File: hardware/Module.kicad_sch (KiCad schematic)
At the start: 47 parts, among them J1 CV_OUT, J10 POWER, J11 RIGHT, J2 CV2, J3 CV1, J4 CV3, J5 CV_TRIGGER, J6 CV_RSNX, J7 CV5, J8 CV4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

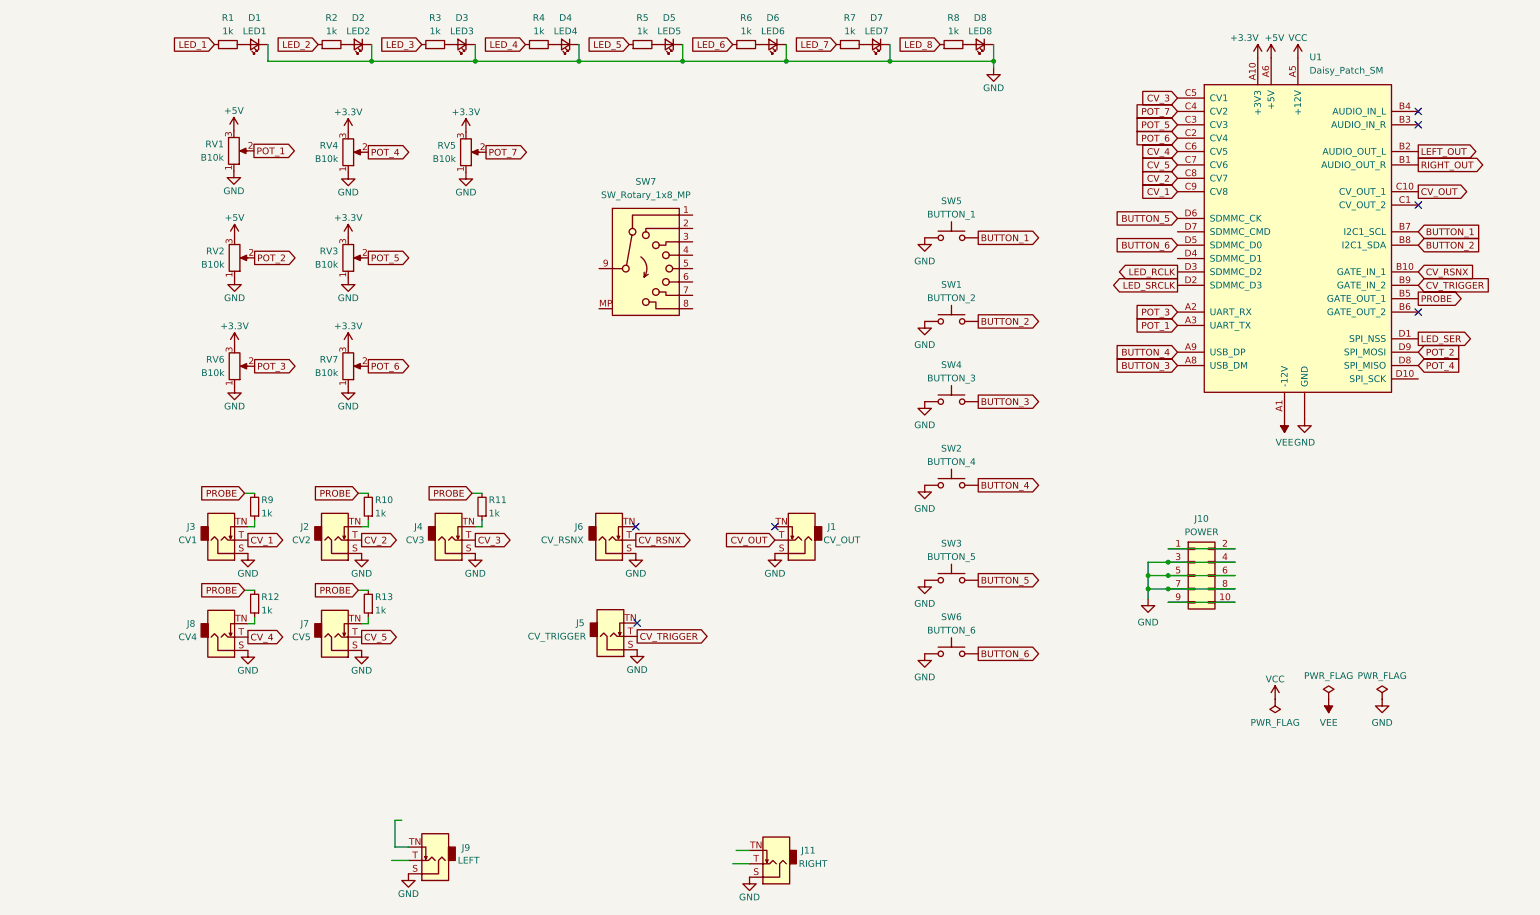
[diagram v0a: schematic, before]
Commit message: Patch a rough schematic
Signed-off-by: Petr Horacek <petr@zlosynth.com>
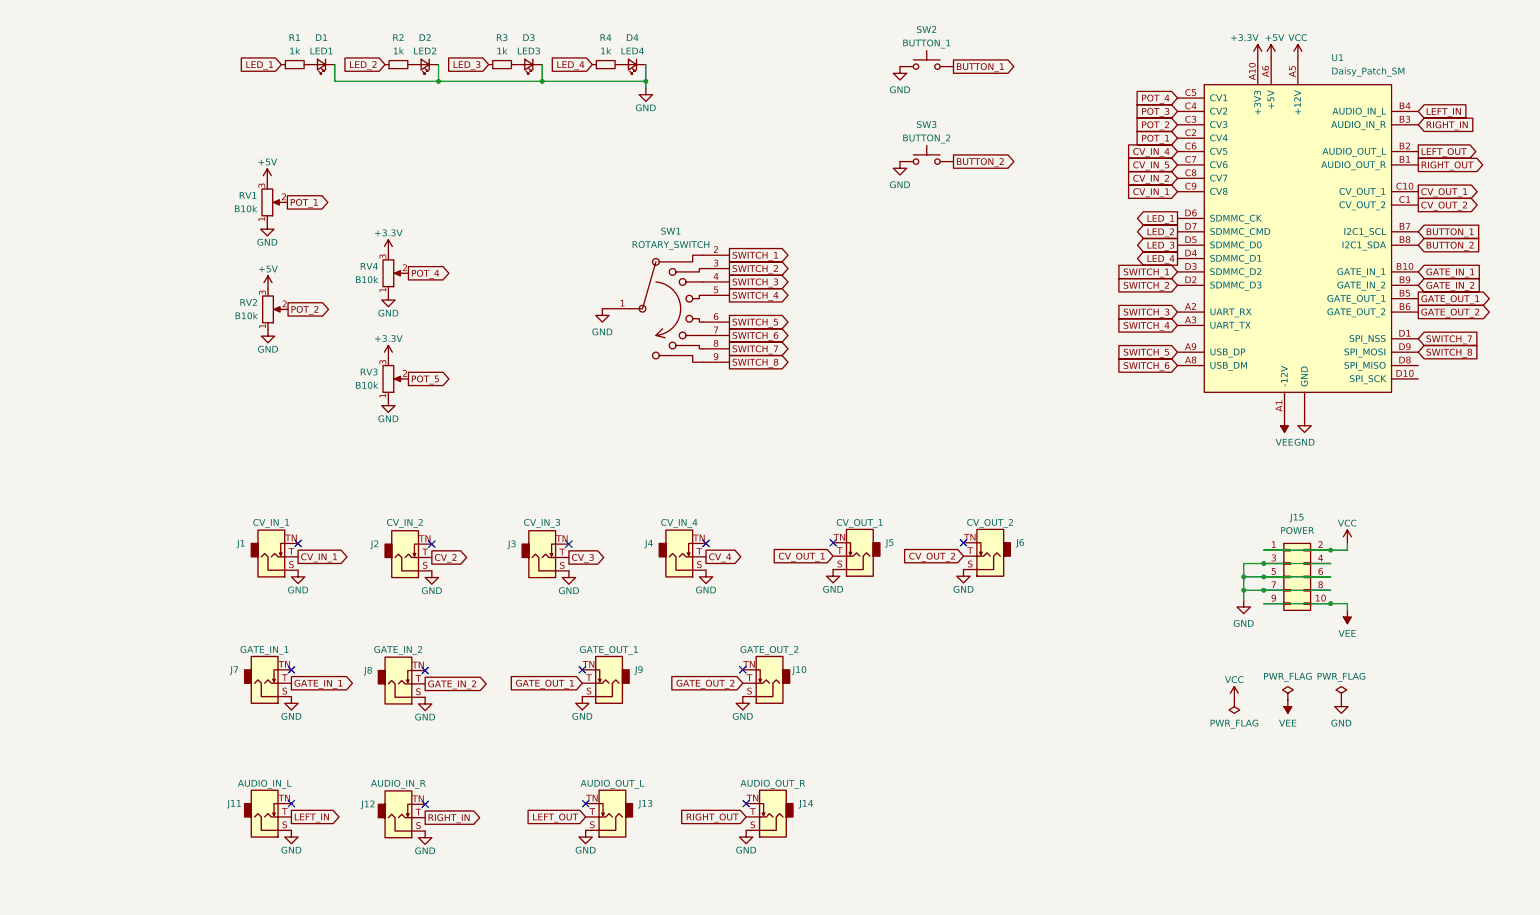
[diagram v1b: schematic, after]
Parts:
- removed D5: LED5, LED_THT:LED_D3.0mm, symbol Device:LED_Small
- removed D6: LED6, LED_THT:LED_D3.0mm, symbol Device:LED_Small
- removed D7: LED7, LED_THT:LED_D3.0mm, symbol Device:LED_Small
- removed D8: LED8, LED_THT:LED_D3.0mm, symbol Device:LED_Small
- removed J1: CV_OUT, Connector_Audio:Jack_3.5mm_QingPu_WQP-PJ398SM_Vertical_CircularHoles, symbol Connector_Audio:AudioJack2_SwitchT
- removed R10, R11, R12, R13, R5, R6, R7, R8, R9: 1k, Resistor_SMD:R_0805_2012Metric_Pad1.20x1.40mm_HandSolder, symbol Device:R_Small
- removed RV5, RV6, RV7: B10k, Custom:Potentiometer_Thonk_Trimmer, symbol Device:R_Potentiometer
- removed SW1: BUTTON_2, Button_Switch_THT:SW_PUSH_6mm, symbol Switch:SW_Push
- removed SW4: BUTTON_3, Button_Switch_THT:SW_PUSH_6mm, symbol Switch:SW_Push
- removed SW5: BUTTON_1, Button_Switch_THT:SW_PUSH_6mm, symbol Switch:SW_Push
- removed SW6: BUTTON_6, Button_Switch_THT:SW_PUSH_6mm, symbol Switch:SW_Push
- removed SW7: SW_Rotary_1x8_MP, Custom:Rotary_Switch_8_Alpha, symbol Switch:SW_Rotary_1x8_MP
- added J10: GATE_OUT_2, Connector_Audio:Jack_3.5mm_QingPu_WQP-PJ398SM_Vertical_CircularHoles, symbol Connector_Audio:AudioJack2_SwitchT
- added J12: AUDIO_IN_R, Connector_Audio:Jack_3.5mm_QingPu_WQP-PJ398SM_Vertical_CircularHoles, symbol Connector_Audio:AudioJack2_SwitchT
- added J13: AUDIO_OUT_L, Connector_Audio:Jack_3.5mm_QingPu_WQP-PJ398SM_Vertical_CircularHoles, symbol Connector_Audio:AudioJack2_SwitchT
- added J14: AUDIO_OUT_R, Connector_Audio:Jack_3.5mm_QingPu_WQP-PJ398SM_Vertical_CircularHoles, symbol Connector_Audio:AudioJack2_SwitchT
- added J8: GATE_IN_2, Connector_Audio:Jack_3.5mm_QingPu_WQP-PJ398SM_Vertical_CircularHoles, symbol Connector_Audio:AudioJack2_SwitchT
- added SW1: ROTARY_SWITCH, Custom:Rotary_Switch_8_Alpha, symbol Custom:SW_Rotary8
- J1: renamed from J3; value CV1 -> CV_IN_1
- J11: value RIGHT -> AUDIO_IN_L
- J2: value CV2 -> CV_IN_2
- J3: renamed from J4; value CV3 -> CV_IN_3
- J4: renamed from J8; value CV4 -> CV_IN_4
- J5: value CV_TRIGGER -> CV_OUT_1
- J6: value CV_RSNX -> CV_OUT_2
- J7: value CV5 -> GATE_IN_1
- J9: value LEFT -> GATE_OUT_1
- SW2: value BUTTON_4 -> BUTTON_1
- SW3: value BUTTON_5 -> BUTTON_2
- renumbered J10 to J15
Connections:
- net BUTTON_6 is gone; now on net LED_3: U1.D5 (SDMMC_D0)
- net POT_6 is gone; now on net POT_1: U1.C2 (CV4)
- net POT_7 is gone; now on net POT_3: U1.C4 (CV2)
- net PROBE is gone; now on net GATE_OUT_1: U1.B5 (GATE_OUT_1)
- net BUTTON_1: now also SW2.2
- net BUTTON_2: now also SW3.2
- net CV_2: no longer U1.C8 (CV7)
- net CV_3: no longer U1.C5 (CV1)
- net CV_4: no longer U1.C6 (CV5)
- net GND: now also J10.S, J12.S, J13.S, J14.S, J8.S, SW1.1
- net LED_1: now also U1.D6 (SDMMC_CK)
- net LED_2: now also U1.D7 (SDMMC_CMD)
- net LED_4: now also U1.D4 (SDMMC_D1)
- net LEFT_OUT: now also J13.T
- net POT_1: no longer U1.A3 (UART_TX)
- net POT_2: now also U1.C3 (CV3); no longer U1.D9 (SPI_MOSI)
- net POT_3: no longer U1.A2 (UART_RX)
- net POT_4: now also U1.C5 (CV1); no longer U1.D8 (SPI_MISO)
- net POT_5: no longer U1.C3 (CV3)
- net RIGHT_OUT: now also J14.T
- net VCC: now also J15.1 (Pin_1), J15.2 (Pin_2)
- net VEE: now also J15.10 (Pin_10), J15.9 (Pin_9)
- net LEFT_IN: now reaches J11.T
- net LEFT_IN: now also U1.B4 (AUDIO_IN_L)
- net RIGHT_IN: now reaches U1.B3 (AUDIO_IN_R)
- net RIGHT_IN: now also J12.T
- net GATE_OUT_2: now reaches U1.B6 (GATE_OUT_2)
- net GATE_OUT_2: now also J10.T
- net CV_OUT_2: now reaches U1.C1 (CV_OUT_2)
- net CV_OUT_2: now also J6.T
- net GATE_OUT_1: now reaches J9.T
- net BUTTON_3 renamed SWITCH_6
- net SWITCH_6: now also SW1.7
- net BUTTON_4 renamed SWITCH_5
- net SWITCH_5: now also SW1.6; no longer SW2.2
- removed net BUTTON_5: SW3.2, U1.D6 (SDMMC_CK)
- net CV_1 renamed CV_IN_1
- net CV_5 renamed CV_IN_5
- net CV_IN_5: no longer J7.T
- net CV_OUT renamed CV_OUT_1
- net CV_OUT_1: now also J5.T
- net CV_RSNX renamed GATE_IN_1
- net GATE_IN_1: now also J7.T; no longer J6.T
- net CV_TRIGGER renamed GATE_IN_2
- net GATE_IN_2: now also J8.T; no longer J5.T
- net LED_RCLK renamed SWITCH_1
- net SWITCH_1: now also SW1.2
- net LED_SER renamed SWITCH_7
- net SWITCH_7: now also SW1.8
- net LED_SRCLK renamed SWITCH_2
- net SWITCH_2: now also SW1.3
- new net CV_IN_2: U1.C8 (CV7)
- new net CV_IN_4: U1.C6 (CV5)
- new net SWITCH_3: SW1.4, U1.A2 (UART_RX)
- new net SWITCH_4: SW1.5, U1.A3 (UART_TX)
- new net SWITCH_8: SW1.9, U1.D9 (SPI_MOSI)
- no-connect marks 7 -> 14
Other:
- title: Arplus -> Handy
- moved on the sheet: D1, D2, D3, D4, J1, J15, J2, J3, J4, R1, R2, R3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

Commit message: First wire up of the PCB
Signed-off-by: Petr Horacek <petr@zlosynth.com>
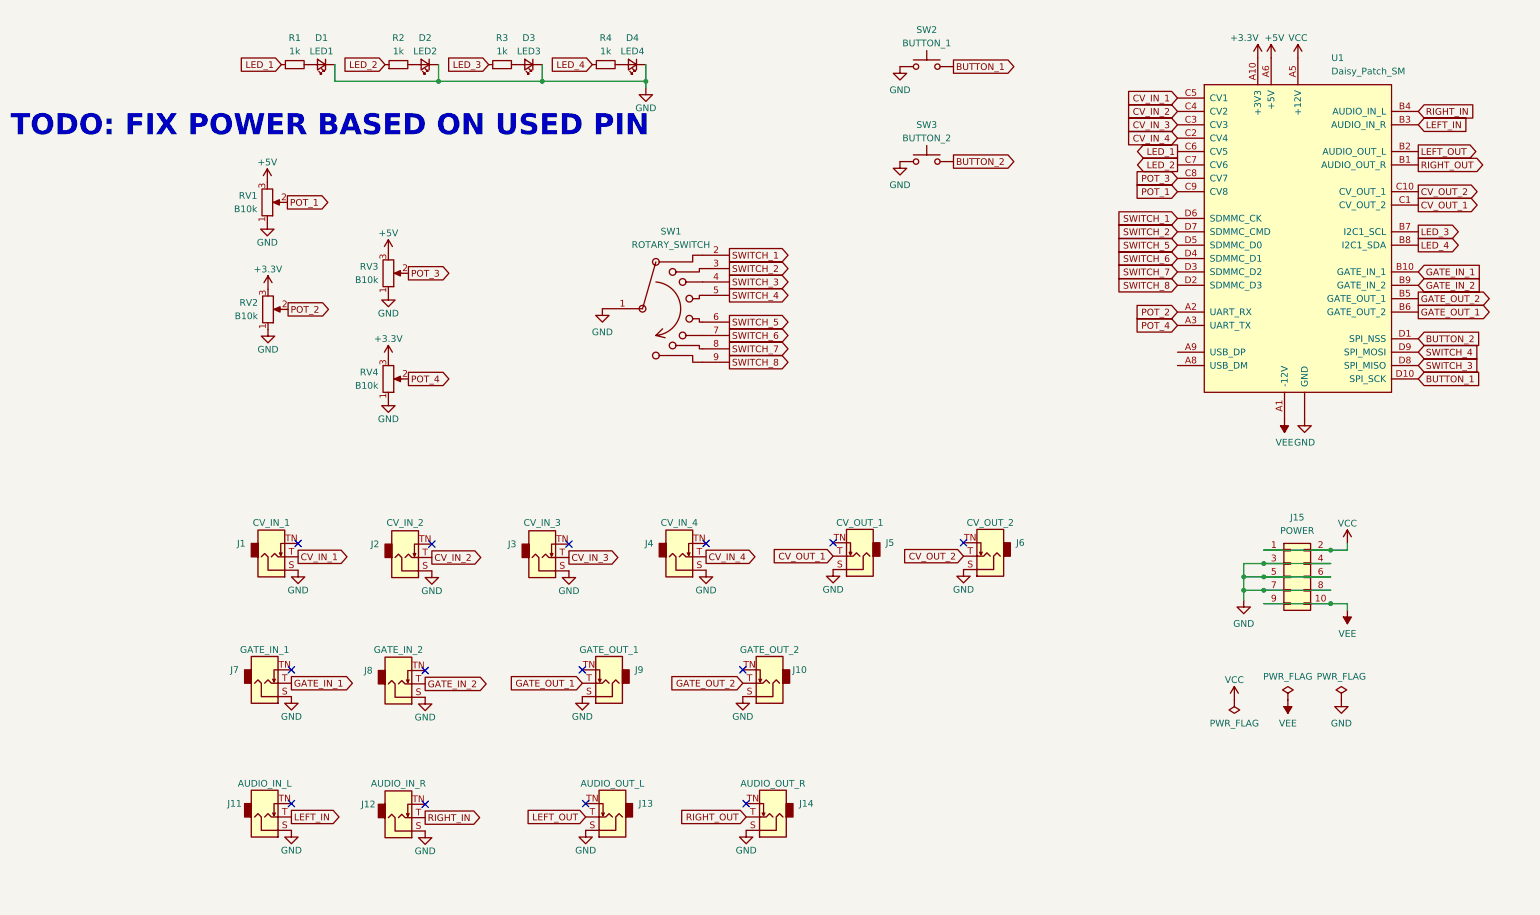
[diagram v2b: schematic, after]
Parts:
- renumbered RV4 to RV3, RV3 to RV4
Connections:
- net CV_2 is gone; now on net CV_IN_2: J2.T
- net CV_4 is gone; now on net CV_IN_4: J4.T
- net CV_IN_5 is gone; now on net LED_2: U1.C7 (CV6)
- net POT_5 is gone; now on net POT_4: RV4.2
- net +3.3V: now also RV2.3; no longer RV3.3
- net +5V: now also RV3.3; no longer RV2.3
- net BUTTON_1: now also U1.D10 (SPI_SCK); no longer U1.B7 (I2C1_SCL)
- net BUTTON_2: now also U1.D1 (SPI_NSS); no longer U1.B8 (I2C1_SDA)
- net CV_IN_1: now also U1.C5 (CV1); no longer U1.C9 (CV8)
- net CV_IN_2: now also U1.C4 (CV2); no longer U1.C8 (CV7)
- net CV_IN_4: now also U1.C2 (CV4); no longer U1.C6 (CV5)
- net CV_OUT_1: now also U1.C1 (CV_OUT_2); no longer U1.C10 (CV_OUT_1)
- net CV_OUT_2: now also U1.C10 (CV_OUT_1); no longer U1.C1 (CV_OUT_2)
- net GATE_OUT_1: now also U1.B6 (GATE_OUT_2); no longer U1.B5 (GATE_OUT_1)
- net GATE_OUT_2: now also U1.B5 (GATE_OUT_1); no longer U1.B6 (GATE_OUT_2)
- net LED_1: now also U1.C6 (CV5); no longer U1.D6 (SDMMC_CK)
- net LED_2: no longer U1.D7 (SDMMC_CMD)
- net LED_3: now also U1.B7 (I2C1_SCL); no longer U1.D5 (SDMMC_D0)
- net LED_4: now also U1.B8 (I2C1_SDA); no longer U1.D4 (SDMMC_D1)
- net LEFT_IN: now also U1.B3 (AUDIO_IN_R); no longer U1.B4 (AUDIO_IN_L)
- net POT_1: now also U1.C9 (CV8); no longer U1.C2 (CV4)
- net POT_2: now also U1.A2 (UART_RX); no longer U1.C3 (CV3)
- net POT_3: now also RV3.2, U1.C8 (CV7); no longer U1.C4 (CV2)
- net POT_4: now also U1.A3 (UART_TX); no longer RV3.2, U1.C5 (CV1)
- net RIGHT_IN: now also U1.B4 (AUDIO_IN_L); no longer U1.B3 (AUDIO_IN_R)
- net SWITCH_1: now also U1.D6 (SDMMC_CK); no longer U1.D3 (SDMMC_D2)
- net SWITCH_2: now also U1.D7 (SDMMC_CMD); no longer U1.D2 (SDMMC_D3)
- net SWITCH_3: now also U1.D8 (SPI_MISO); no longer U1.A2 (UART_RX)
- net SWITCH_4: now also U1.D9 (SPI_MOSI); no longer U1.A3 (UART_TX)
- net SWITCH_5: now also U1.D5 (SDMMC_D0); no longer U1.A9 (USB_DP)
- net SWITCH_6: now also U1.D4 (SDMMC_D1); no longer U1.A8 (USB_DM)
- net SWITCH_7: now also U1.D3 (SDMMC_D2); no longer U1.D1 (SPI_NSS)
- net SWITCH_8: now also U1.D2 (SDMMC_D3); no longer U1.D9 (SPI_MOSI)
- net CV_3 renamed CV_IN_3
- net CV_IN_3: now also U1.C3 (CV3)
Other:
- note added: "TODO: FIX POWER BASED ON USED PIN"

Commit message: Complete the ground plane and fix ERC
Signed-off-by: Petr Horacek <petr@zlosynth.com>
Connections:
- no-connect marks 14 -> 16
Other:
- note removed: "TODO: FIX POWER BASED ON USED PIN"

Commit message: Fix trimmer footprint
Signed-off-by: Petr Horacek <petr@zlosynth.com>
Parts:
- RV1, RV3: footprint Potentiometer_THT:Potentiometer_Alpha_RD901F-40-00D_Single_Vertical -> Custom:Potentiometer_Thonk_Trimmer
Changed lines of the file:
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@@
       (effects (font (size 1.27 1.27)) (justify right))
     )
-    (property "Footprint" "Potentiometer_THT:Potentiometer_Alpha_RD901F-40-00D_Single_Vertical" (at 34.163 56.007 0)
+    (property "Footprint" "Custom:Potentiometer_Thonk_Trimmer" (at 34.163 56.007 0)
       (effects (font (size 1.27 1.27)) hide)
     )
@@
       (effects (font (size 1.27 1.27)) (justify right))
     )
-    (property "Footprint" "Potentiometer_THT:Potentiometer_Alpha_RD901F-40-00D_Single_Vertical" (at 57.15 69.469 0)
-      (effects (font (size 1.27 1.27)) hide)
-    )
+    (property "Footprint" "Custom:Potentiometer_Thonk_Trimmer" (at 57.15 69.469 0)
+      (effects (font (size 1.27 1.27)) hide)
+    )

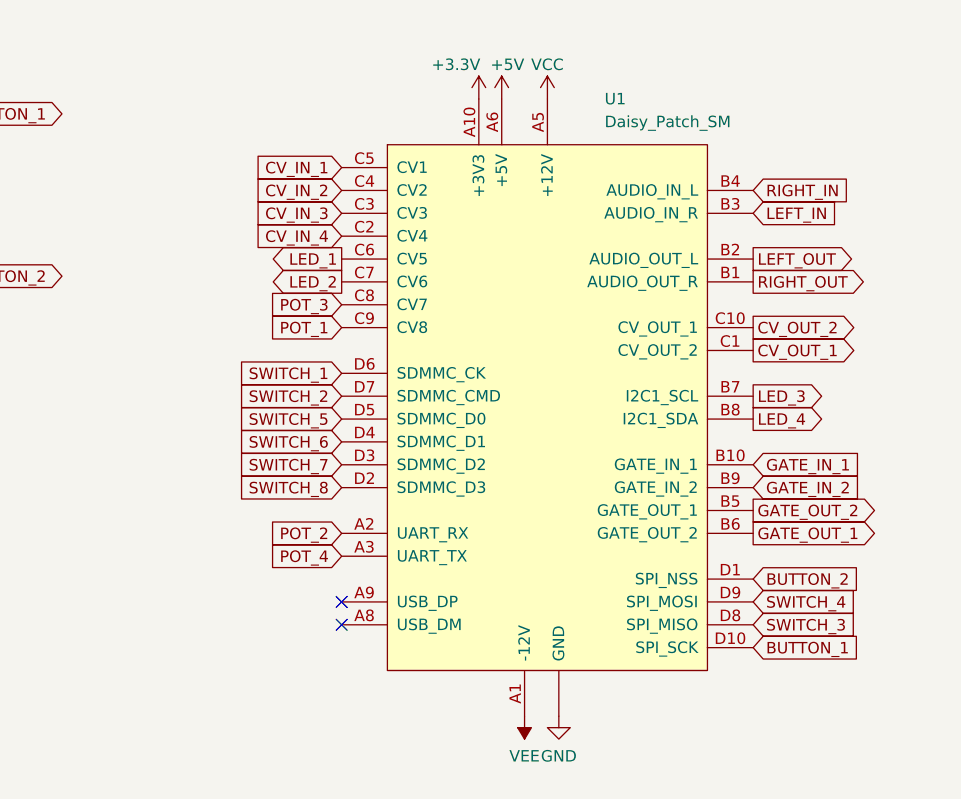
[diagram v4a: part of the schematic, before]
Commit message: Fix LED daisy connection
Signed-off-by: Petr Horacek <petr@zlosynth.com>
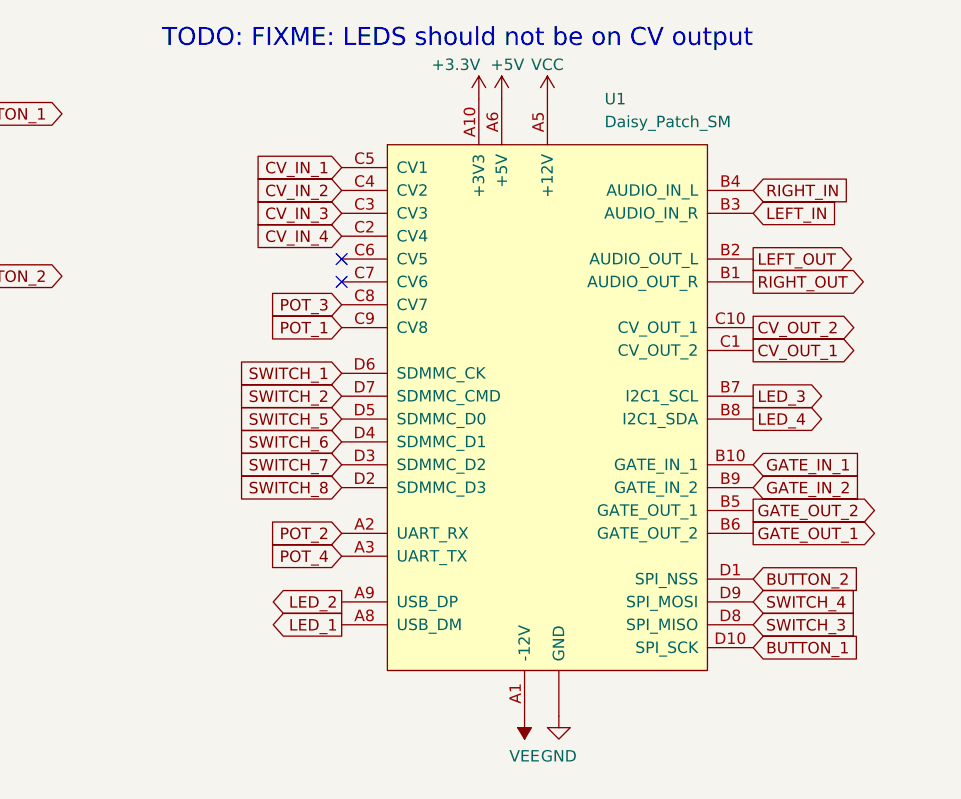
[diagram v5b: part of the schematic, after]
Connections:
- net LED_1: now also U1.A8 (USB_DM); no longer U1.C6 (CV5)
- net LED_2: now also U1.A9 (USB_DP); no longer U1.C7 (CV6)
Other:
- note added: "TODO: FIXME: LEDS should not be on CV output"
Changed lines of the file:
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@@
   (no_connect (at 141.732 120.65))
   (no_connect (at 64.262 170.434))
+  (no_connect (at 207.01 48.895))
   (no_connect (at 117.602 120.904))
   (no_connect (at 40.132 120.904))
+  (no_connect (at 207.01 46.355))
   (no_connect (at 65.532 120.904))
-  (no_connect (at 207.01 84.455))
   (no_connect (at 91.44 120.904))
   (no_connect (at 166.37 120.65))
   (no_connect (at 64.262 145.034))
   (no_connect (at 38.862 144.78))
-  (no_connect (at 207.01 86.995))
   (no_connect (at 124.46 144.78))
   (no_connect (at 125.222 170.18))
@@
     (stroke (width 0) (type default))
   )
+  (text "TODO: FIXME: LEDS should not be on CV output" (at 187.0456 23.0632 0)
+    (effects (font (size 2 2)) (justify left bottom))
+  )
   (global_label "SWITCH_6" (shape output) (at 121.92 81.28 0) (fields_autoplaced)
     (effects (font (size 1.27 1.27)) (justify left))
@@
     )
   )
-  (global_label "LED_1" (shape output) (at 207.01 46.355 180) (fields_autoplaced)
-    (effects (font (size 1.27 1.27)) (justify right))
-    (property "Intersheetrefs" "${INTERSHEET_REFS}" (at 198.4006 46.355 0)
+  (global_label "LED_1" (shape output) (at 207.01 86.995 180) (fields_autoplaced)
+    (effects (font (size 1.27 1.27)) (justify right))
+    (property "Intersheetrefs" "${INTERSHEET_REFS}" (at 198.4006 86.995 0)
       (effects (font (size 1.27 1.27)) (justify right) hide)
     )
@@
     )
   )
-  (global_label "LED_2" (shape output) (at 207.01 48.895 180) (fields_autoplaced)
-    (effects (font (size 1.27 1.27)) (justify right))
-    (property "Intersheetrefs" "${INTERSHEET_REFS}" (at 198.4006 48.895 0)
-      (effects (font (size 1.27 1.27)) (justify right) hide)
-    )
+  (global_label "LED_2" (shape output) (at 207.01 84.455 180) (fields_autoplaced)
+    (effects (font (size 1.27 1.27)) (justify right))
+    (property "Intersheetrefs" "${INTERSHEET_REFS}" (at 198.4006 84.455 0)
+      (effects (font (size 1.27 1.27)) (justify right) hide)
+    )
